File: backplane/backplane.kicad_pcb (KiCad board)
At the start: 2 copper layers, 2 parts, among them J2 Conn_01x10_Pin

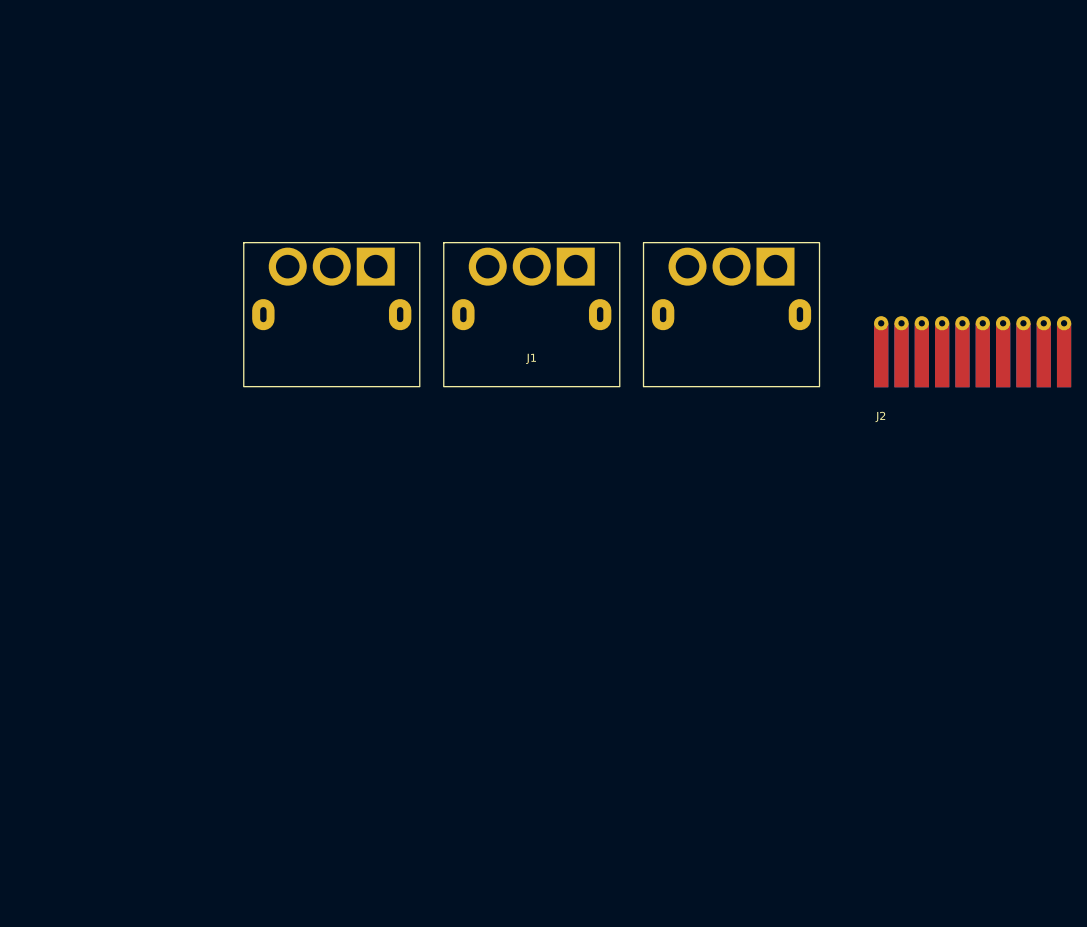
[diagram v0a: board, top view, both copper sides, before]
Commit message: finalized backplane schematic, started pcb layout
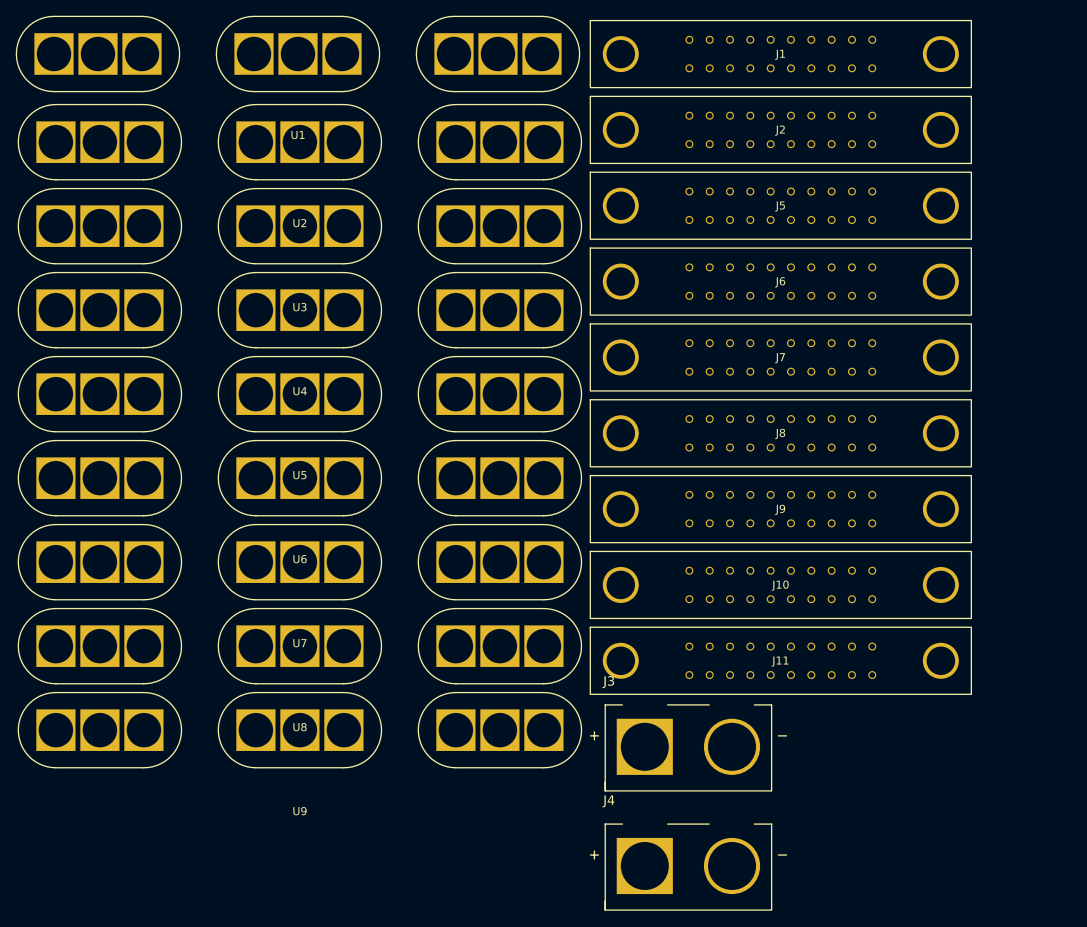
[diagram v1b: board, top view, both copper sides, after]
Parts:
- added J10: Conn_01x10, 2024-backplane:EDAC_Edge_2x10, F.Cu at (139.9, 102.4)
- added J11: Conn_01x10, 2024-backplane:EDAC_Edge_2x10, F.Cu at (139.9, 111.8)
- added J3: 48V in, 2024-backplane:AMASS_XT90PW-M_MOD_NUMS, F.Cu at (128.3, 130.7)
- added J4: 48V in, 2024-backplane:AMASS_XT90PW-M_MOD_NUMS, F.Cu at (128.3, 145.6)
- added J5: Conn_01x10, 2024-backplane:EDAC_Edge_2x10, F.Cu at (139.9, 55.0)
- added J6: Conn_01x10, 2024-backplane:EDAC_Edge_2x10, F.Cu at (139.9, 64.5)
- added J7: Conn_01x10, 2024-backplane:EDAC_Edge_2x10, F.Cu at (139.9, 73.9)
- added J8: Conn_01x10, 2024-backplane:EDAC_Edge_2x10, F.Cu at (139.9, 83.4)
- added J9: Conn_01x10, 2024-backplane:EDAC_Edge_2x10, F.Cu at (139.9, 92.9)
- added U1: ~, 2024-backplane:MR60-F_X3, F.Cu at (79.5, 36.0)
- added U2: ~, 2024-backplane:MR60-F_X3, F.Cu at (79.7, 47.0)
- added U3: ~, 2024-backplane:MR60-F_X3, F.Cu at (79.7, 57.5)
- added U4: ~, 2024-backplane:MR60-F_X3, F.Cu at (79.7, 68.0)
- added U5: ~, 2024-backplane:MR60-F_X3, F.Cu at (79.7, 78.5)
- added U6: ~, 2024-backplane:MR60-F_X3, F.Cu at (79.7, 89.0)
- added U7: ~, 2024-backplane:MR60-F_X3, F.Cu at (79.7, 99.5)
- added U8: ~, 2024-backplane:MR60-F_X3, F.Cu at (79.7, 110.0)
- added U9: ~, 2024-backplane:MR60-F_X3, F.Cu at (79.7, 120.5)
- J1: value ~ -> Conn_01x10; footprint 2024-backplane:MR60PW-M_X3 -> 2024-backplane:EDAC_Edge_2x10
- J2: value Conn_01x10_Pin -> Conn_01x10; footprint 2024-backplane:CardEdge_2x10 -> 2024-backplane:EDAC_Edge_2x10
- moved J1 40.9 mm to (139.9, 36.0)
- moved J2 30.8 mm to (139.9, 45.5)
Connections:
- J1 pad 1: unconnected-(J1A-A-Pad1) -> /a
- J1 pad 2: unconnected-(J1A-B-Pad2) -> /b
- J1 pad 3: unconnected-(J1A-C-Pad3) -> /c
- J1 pad 4: unconnected-(J1B-A-Pad4) -> /d
- J1 pad 5: unconnected-(J1B-B-Pad5) -> /e
- J1 pad 6: unconnected-(J1B-C-Pad6) -> /f
- J1 pad 7: unconnected-(J1C-A-Pad7) -> /g
- J1 pad 8: unconnected-(J1C-B-Pad8) -> /h
- J1 pad 9: unconnected-(J1C-C-Pad9) -> /i
- J2 pad 1: unconnected-(J2-Pin_1-Pad1) -> /a
- J2 pad 10: unconnected-(J2-Pin_10-Pad10) -> /j
- J2 pad 2: unconnected-(J2-Pin_2-Pad2) -> /b
- J2 pad 3: unconnected-(J2-Pin_3-Pad3) -> /c
- J2 pad 4: unconnected-(J2-Pin_4-Pad4) -> /d
- J2 pad 5: unconnected-(J2-Pin_5-Pad5) -> /e
- J2 pad 6: unconnected-(J2-Pin_6-Pad6) -> /f
- J2 pad 7: unconnected-(J2-Pin_7-Pad7) -> /g
- J2 pad 8: unconnected-(J2-Pin_8-Pad8) -> /h
- J2 pad 9: unconnected-(J2-Pin_9-Pad9) -> /i

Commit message: yes
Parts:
- moved J1 2.79 mm to (139.9, 33.2)
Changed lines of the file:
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@@
   )
   (footprint "2024-backplane:EDAC_Edge_2x10" (layer "F.Cu")
-    (at 139.855 36.01)
+    (at 139.855 33.22)
     (property "Sheetfile" "backplane.kicad_sch")
     (property "Sheetname" "")

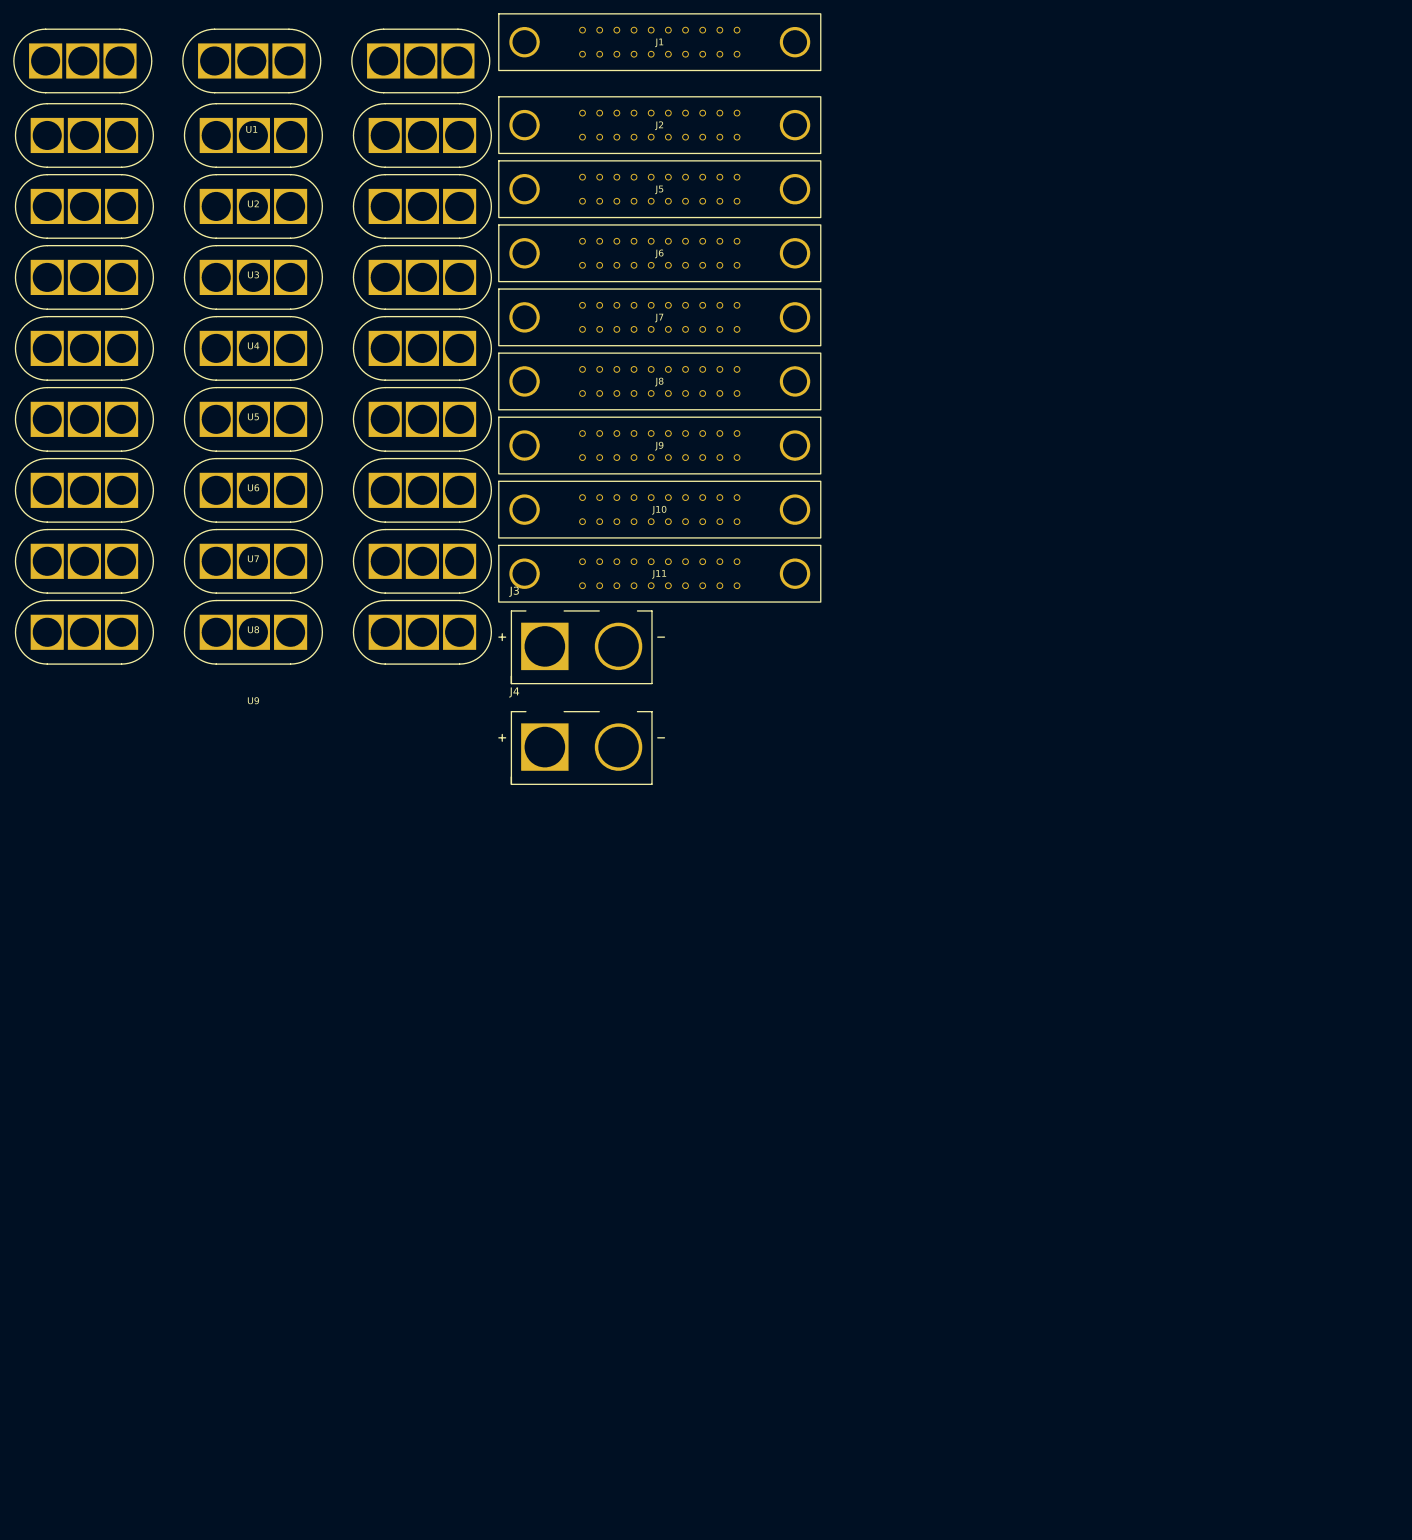
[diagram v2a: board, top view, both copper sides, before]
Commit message: backplane is laid out
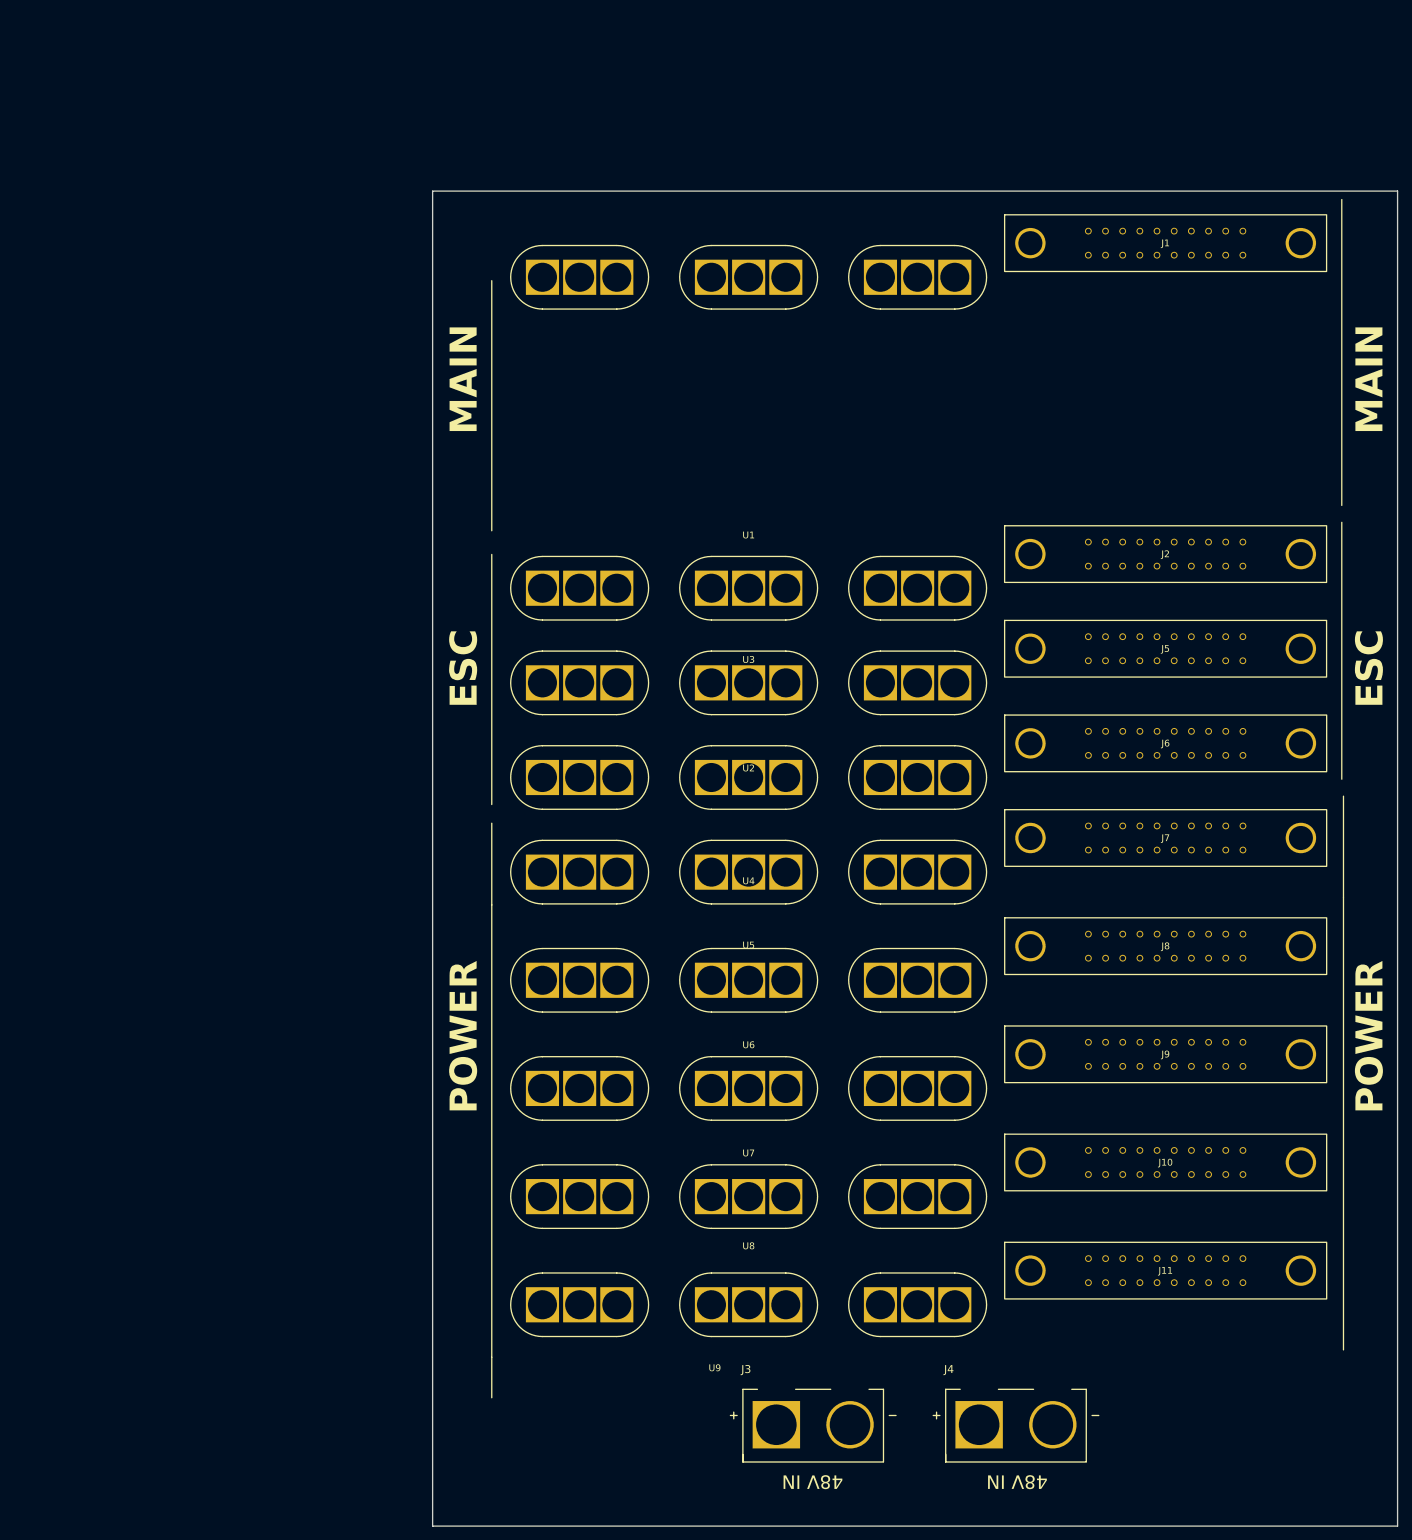
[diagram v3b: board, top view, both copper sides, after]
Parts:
- moved J11 127.4 mm to (214.7, 214.9)
- moved U9 123.5 mm to (153.0, 220.0)
- moved J10 122.2 mm to (214.7, 198.9)
- moved U8 119.2 mm to (153.0, 204.0)
- moved J9 117.1 mm to (214.7, 182.9)
- moved U7 114.9 mm to (153.0, 188.0)
- moved J3 112.6 mm to (162.8, 237.9)
- moved J4 112.6 mm to (192.8, 237.9)
- moved J8 112.2 mm to (214.7, 166.9)
- moved U6 110.7 mm to (153.0, 172.0)
- moved J7 107.4 mm to (214.7, 150.9)
- moved U5 106.6 mm to (153.0, 156.0)
- moved J6 104.2 mm to (214.7, 136.9)
- moved U4 104.1 mm to (153.0, 142.0)
- moved U3 101.7 mm to (153.0, 128.0)
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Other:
- board outline added: 142.8 x 197.5 mm
- board text added: "48V IN"
- board text added: "ESC"
- board text added: "MAIN"
- board text added: "POWER"

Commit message: backplane routed
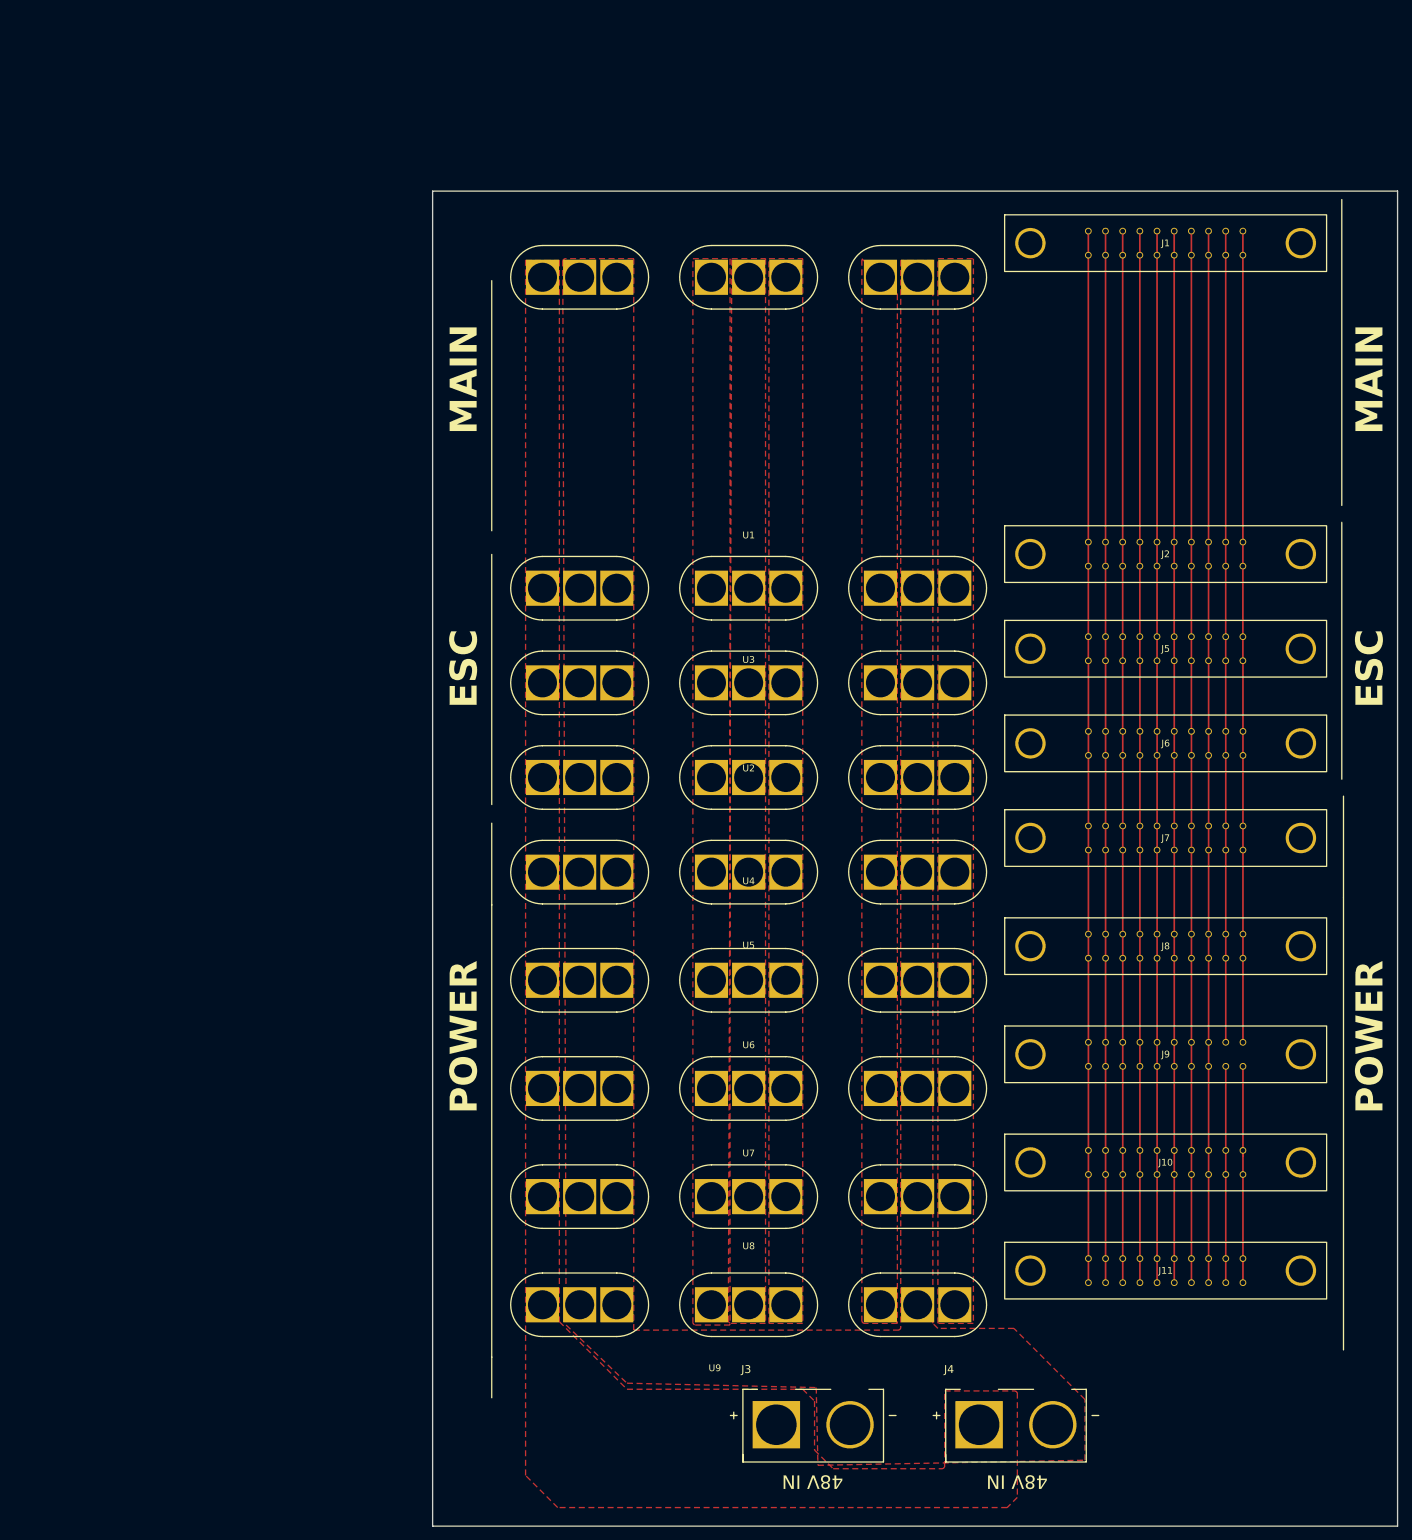
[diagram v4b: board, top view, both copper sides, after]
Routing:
- net /h: track 0.00 -> 156.1 mm
- net /b: track 0.00 -> 156.0 mm
- net /f: track 0.00 -> 155.6 mm
- net /g: track 0.00 -> 155.6 mm
- net /d: track 0.00 -> 155.6 mm
- net /c: track 0.00 -> 155.6 mm
- net /a: track 0.00 -> 155.6 mm
- net /e: track 0.00 -> 155.2 mm
- net /j: track 0.00 -> 152.8 mm
- net /i: track 0.00 -> 152.0 mm
- added copper zone on F.Cu, net /12v_1
- added copper zone on F.Cu, net /12v_2
- added copper zone on F.Cu, net /12v_3
- added copper zone on F.Cu, net /24v
- added copper zone on F.Cu, net /48v
- added copper zone on F.Cu, net /5v
- added copper zone on F.Cu, net GND1
